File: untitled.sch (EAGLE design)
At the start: 38 parts, among them J2 1x3 RA Female .1", J3 CORTEX_DEBUG_PTH

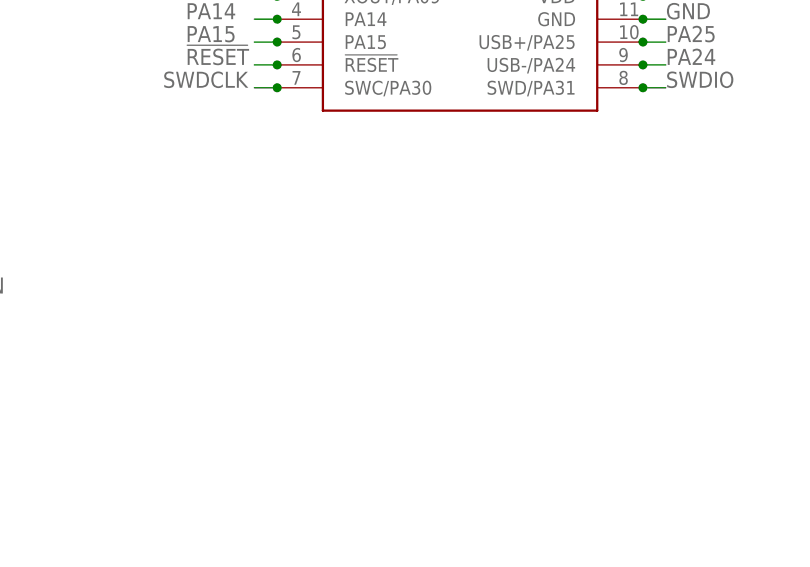
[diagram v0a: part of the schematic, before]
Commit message: Added USB connector
added USB connector for debugging, dropped to 4 layer board
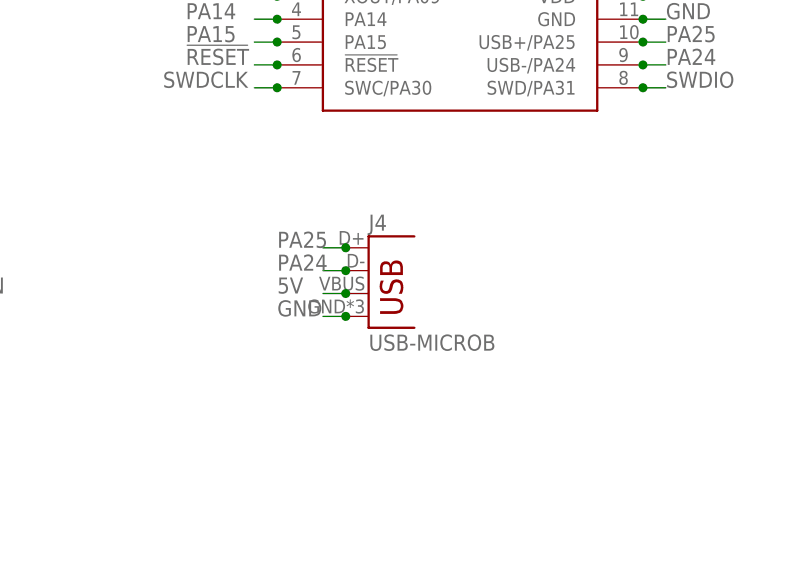
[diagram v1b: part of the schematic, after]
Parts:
- added J4: USB-MICROB, SparkFun-Retired:USB-MICROB
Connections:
- net 5V: now also J4.VBUS
- net GND: now also J4.GND
- net PA24: now also J4.D-
- net PA25: now also J4.D+
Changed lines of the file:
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@@
 <part name="R7" library="resistor" library_urn="urn:adsk.eagle:library:348" deviceset="R-US_" device="R0402" package3d_urn="urn:adsk.eagle:package:26058/1" value="100k"/>
 <part name="L7" library="SparkFun-Coils" library_urn="urn:adsk.eagle:library:512" deviceset="INDUCTOR" device="-0603-33NH" package3d_urn="urn:adsk.eagle:package:37574/1" value="68nH"/>
+<part name="J4" library="SparkFun-Retired" library_urn="urn:adsk.eagle:library:533" deviceset="USB" device="-MICROB"/>
 </parts>
 <sheets>
@@
 <instance part="R7" gate="G$1" x="218.44" y="22.86" rot="R180"/>
 <instance part="L7" gate="G$1" x="266.7" y="68.58" rot="R90"/>
+<instance part="J4" gate="G$1" x="160.02" y="96.52"/>
 </instances>
 <busses>
@@
 <wire x1="271.78" y1="68.58" x2="274.32" y2="68.58" width="0.1524" layer="91"/>
 <junction x="271.78" y="68.58"/>
+</segment>
+<segment>
+<pinref part="J4" gate="G$1" pin="GND"/>
+<wire x1="157.48" y1="96.52" x2="154.94" y2="96.52" width="0.1524" layer="91"/>
+<junction x="157.48" y="96.52"/>
+<label x="149.86" y="96.52" size="1.778" layer="95"/>
 </segment>
 </net>
@@
 <junction x="124.46" y="45.72"/>
 </segment>
+<segment>
+<pinref part="J4" gate="G$1" pin="D+"/>
+<wire x1="157.48" y1="104.14" x2="154.94" y2="104.14" width="0.1524" layer="91"/>
+<junction x="157.48" y="104.14"/>
+<label x="149.86" y="104.14" size="1.778" layer="95"/>
+</segment>
 </net>
 <net name="PA24" class="0">
@@
 <junction x="124.46" y="48.26"/>
 </segment>
+<segment>
+<pinref part="J4" gate="G$1" pin="D-"/>
+<wire x1="157.48" y1="101.6" x2="154.94" y2="101.6" width="0.1524" layer="91"/>
+<junction x="157.48" y="101.6"/>
+<label x="149.86" y="101.6" size="1.778" layer="95"/>
+</segment>
 </net>
 <net name="5V" class="0">
@@
 <junction x="223.52" y="22.86"/>
 </segment>
-</net>
+<segment>
+<pinref part="J4" gate="G$1" pin="VBUS"/>
+<wire x1="157.48" y1="99.06" x2="154.94" y2="99.06" width="0.1524" layer="91"/>
+<junction x="157.48" y="99.06"/>
+<label x="149.86" y="99.06" size="1.778" layer="95"/>
+</segment>
+</net>

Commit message: Added test points to SI4464
Added test points to unused pins for later use. Cleaned up routing.
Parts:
- added TP1, TP2, TP3, TP4, TP5: TEST-POINT3, SparkFun-Connectors:TEST-POINT3
- C1: value (none) -> 12pf
- C2: value (none) -> 470pf
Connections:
- net GPIO0: now also TP2.1
- net GPIO2: now also TP4.1
- net GPIO3: now also TP5.1
- net NIRQ: now also TP3.1
- net TXRAMP: now also TP1.1
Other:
- moved on the sheet: C1, C10, C2, C3, C4, C5, C6, C7, C8, C9, J1, J2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

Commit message: Added 0 ohm resistors to spi
added 0 ohm jumpers between spi pins on the micro and si4464
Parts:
- added R10, R11, R8, R9: 0, resistor:R-US_R0402
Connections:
- new net PA241: R10.1, U$2.SDO
- new net PA251: R11.1, U$2.SCLK
- new net SWDCLK1: R8.1, U$2.NSEL
- new net SWDIO1: R9.1, U$2.SDI
- net PA24: now also R10.2; no longer U$2.SDO
- net PA25: now also R11.2; no longer U$2.SCLK
- net SWDCLK: now also R8.2; no longer U$2.NSEL
- net SWDIO: now also R9.2; no longer U$2.SDI
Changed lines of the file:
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@@
 <part name="TP4" library="SparkFun-Connectors" library_urn="urn:adsk.eagle:library:513" deviceset="TEST-POINT" device="3" package3d_urn="urn:adsk.eagle:package:38286/1"/>
 <part name="TP5" library="SparkFun-Connectors" library_urn="urn:adsk.eagle:library:513" deviceset="TEST-POINT" device="3" package3d_urn="urn:adsk.eagle:package:38286/1"/>
+<part name="R8" library="resistor" library_urn="urn:adsk.eagle:library:348" deviceset="R-US_" device="R0402" package3d_urn="urn:adsk.eagle:package:26058/1" value="0"/>
+<part name="R9" library="resistor" library_urn="urn:adsk.eagle:library:348" deviceset="R-US_" device="R0402" package3d_urn="urn:adsk.eagle:package:26058/1" value="0"/>
+<part name="R10" library="resistor" library_urn="urn:adsk.eagle:library:348" deviceset="R-US_" device="R0402" package3d_urn="urn:adsk.eagle:package:26058/1" value="0"/>
+<part name="R11" library="resistor" library_urn="urn:adsk.eagle:library:348" deviceset="R-US_" device="R0402" package3d_urn="urn:adsk.eagle:package:26058/1" value="0"/>
 </parts>
 <sheets>
@@
 <instance part="TP4" gate="G$1" x="-93.98" y="132.08" rot="R90"/>
 <instance part="TP5" gate="G$1" x="-86.36" y="132.08" rot="R90"/>
+<instance part="R8" gate="G$1" x="-53.34" y="152.4"/>
+<instance part="R9" gate="G$1" x="-53.34" y="144.78"/>
+<instance part="R10" gate="G$1" x="-53.34" y="137.16"/>
+<instance part="R11" gate="G$1" x="-53.34" y="129.54"/>
 </instances>
 <busses>
@@
 </segment>
 <segment>
-<pinref part="U$2" gate="G$1" pin="SDI"/>
-<wire x1="-78.74" y1="185.42" x2="-76.2" y2="185.42" width="0.1524" layer="91"/>
-<label x="-76.2" y="185.42" size="1.778" layer="95"/>
-<junction x="-78.74" y="185.42"/>
+<pinref part="R9" gate="G$1" pin="2"/>
+<wire x1="-48.26" y1="144.78" x2="-45.72" y2="144.78" width="0.1524" layer="91"/>
+<junction x="-48.26" y="144.78"/>
+<label x="-43.18" y="144.78" size="1.778" layer="95"/>
 </segment>
 </net>
@@
 </segment>
 <segment>
-<pinref part="U$2" gate="G$1" pin="NSEL"/>
-<wire x1="-78.74" y1="187.96" x2="-76.2" y2="187.96" width="0.1524" layer="91"/>
-<label x="-76.2" y="187.96" size="1.778" layer="95"/>
-<junction x="-78.74" y="187.96"/>
+<pinref part="R8" gate="G$1" pin="2"/>
+<wire x1="-48.26" y1="152.4" x2="-45.72" y2="152.4" width="0.1524" layer="91"/>
+<junction x="-48.26" y="152.4"/>
+<label x="-43.18" y="152.4" size="1.778" layer="95"/>
 </segment>
 </net>
@@
 </segment>
 <segment>
-<pinref part="U$2" gate="G$1" pin="SCLK"/>
-<wire x1="-78.74" y1="180.34" x2="-76.2" y2="180.34" width="0.1524" layer="91"/>
-<label x="-76.2" y="180.34" size="1.778" layer="95"/>
-<junction x="-78.74" y="180.34"/>
-</segment>
-<segment>
 <pinref part="J4" gate="G$1" pin="D+"/>
 <wire x1="-172.72" y1="33.02" x2="-172.72" y2="35.56" width="0.1524" layer="91"/>
@@
 <label x="-172.72" y="40.64" size="1.778" layer="95" rot="R270"/>
 </segment>
+<segment>
+<pinref part="R11" gate="G$1" pin="2"/>
+<wire x1="-48.26" y1="129.54" x2="-45.72" y2="129.54" width="0.1524" layer="91"/>
+<junction x="-48.26" y="129.54"/>
+<label x="-43.18" y="129.54" size="1.778" layer="95"/>
+</segment>
 </net>
 <net name="PA24" class="0">
@@
 </segment>
 <segment>
-<pinref part="U$2" gate="G$1" pin="SDO"/>
-<wire x1="-78.74" y1="182.88" x2="-76.2" y2="182.88" width="0.1524" layer="91"/>
-<label x="-76.2" y="182.88" size="1.778" layer="95"/>
-<junction x="-78.74" y="182.88"/>
-</segment>
-<segment>
 <pinref part="J4" gate="G$1" pin="D-"/>
 <wire x1="-175.26" y1="33.02" x2="-175.26" y2="35.56" width="0.1524" layer="91"/>
 <junction x="-175.26" y="33.02"/>
 <label x="-175.26" y="40.64" size="1.778" layer="95" rot="R270"/>
+</segment>
+<segment>
+<pinref part="R10" gate="G$1" pin="2"/>
+<wire x1="-48.26" y1="137.16" x2="-45.72" y2="137.16" width="0.1524" layer="91"/>
+<junction x="-48.26" y="137.16"/>
+<label x="-43.18" y="137.16" size="1.778" layer="95"/>
 </segment>
 </net>
@@
 </segment>
 </net>
+<net name="SWDCLK1" class="0">
+<segment>
+<pinref part="U$2" gate="G$1" pin="NSEL"/>
+<wire x1="-78.74" y1="187.96" x2="-76.2" y2="187.96" width="0.1524" layer="91"/>
+<label x="-76.2" y="187.96" size="1.778" layer="95"/>
+<junction x="-78.74" y="187.96"/>
+</segment>
+<segment>
+<pinref part="R8" gate="G$1" pin="1"/>
+<wire x1="-58.42" y1="152.4" x2="-60.96" y2="152.4" width="0.1524" layer="91"/>
+<junction x="-58.42" y="152.4"/>
+<label x="-73.66" y="152.4" size="1.778" layer="95"/>
+</segment>
+</net>
+<net name="SWDIO1" class="0">
+<segment>
+<pinref part="U$2" gate="G$1" pin="SDI"/>
+<wire x1="-78.74" y1="185.42" x2="-76.2" y2="185.42" width="0.1524" layer="91"/>
+<label x="-76.2" y="185.42" size="1.778" layer="95"/>
+<junction x="-78.74" y="185.42"/>
+</segment>
+<segment>
+<pinref part="R9" gate="G$1" pin="1"/>
+<wire x1="-58.42" y1="144.78" x2="-60.96" y2="144.78" width="0.1524" layer="91"/>
+<junction x="-58.42" y="144.78"/>
+<label x="-73.66" y="144.78" size="1.778" layer="95"/>
+</segment>
+</net>
+<net name="PA241" class="0">
+<segment>
+<pinref part="U$2" gate="G$1" pin="SDO"/>
+<wire x1="-78.74" y1="182.88" x2="-76.2" y2="182.88" width="0.1524" layer="91"/>
+<label x="-76.2" y="182.88" size="1.778" layer="95"/>
+<junction x="-78.74" y="182.88"/>
+</segment>
+<segment>
+<pinref part="R10" gate="G$1" pin="1"/>
+<wire x1="-58.42" y1="137.16" x2="-60.96" y2="137.16" width="0.1524" layer="91"/>
+<junction x="-58.42" y="137.16"/>
+<label x="-73.66" y="137.16" size="1.778" layer="95"/>
+</segment>
+</net>
+<net name="PA251" class="0">
+<segment>
+<pinref part="U$2" gate="G$1" pin="SCLK"/>
+<wire x1="-78.74" y1="180.34" x2="-76.2" y2="180.34" width="0.1524" layer="91"/>
+<label x="-76.2" y="180.34" size="1.778" layer="95"/>
+<junction x="-78.74" y="180.34"/>
+</segment>
+<segment>
+<pinref part="R11" gate="G$1" pin="1"/>
+<wire x1="-58.42" y1="129.54" x2="-60.96" y2="129.54" width="0.1524" layer="91"/>
+<junction x="-58.42" y="129.54"/>
+<label x="-73.66" y="129.54" size="1.778" layer="95"/>
+</segment>
+</net>

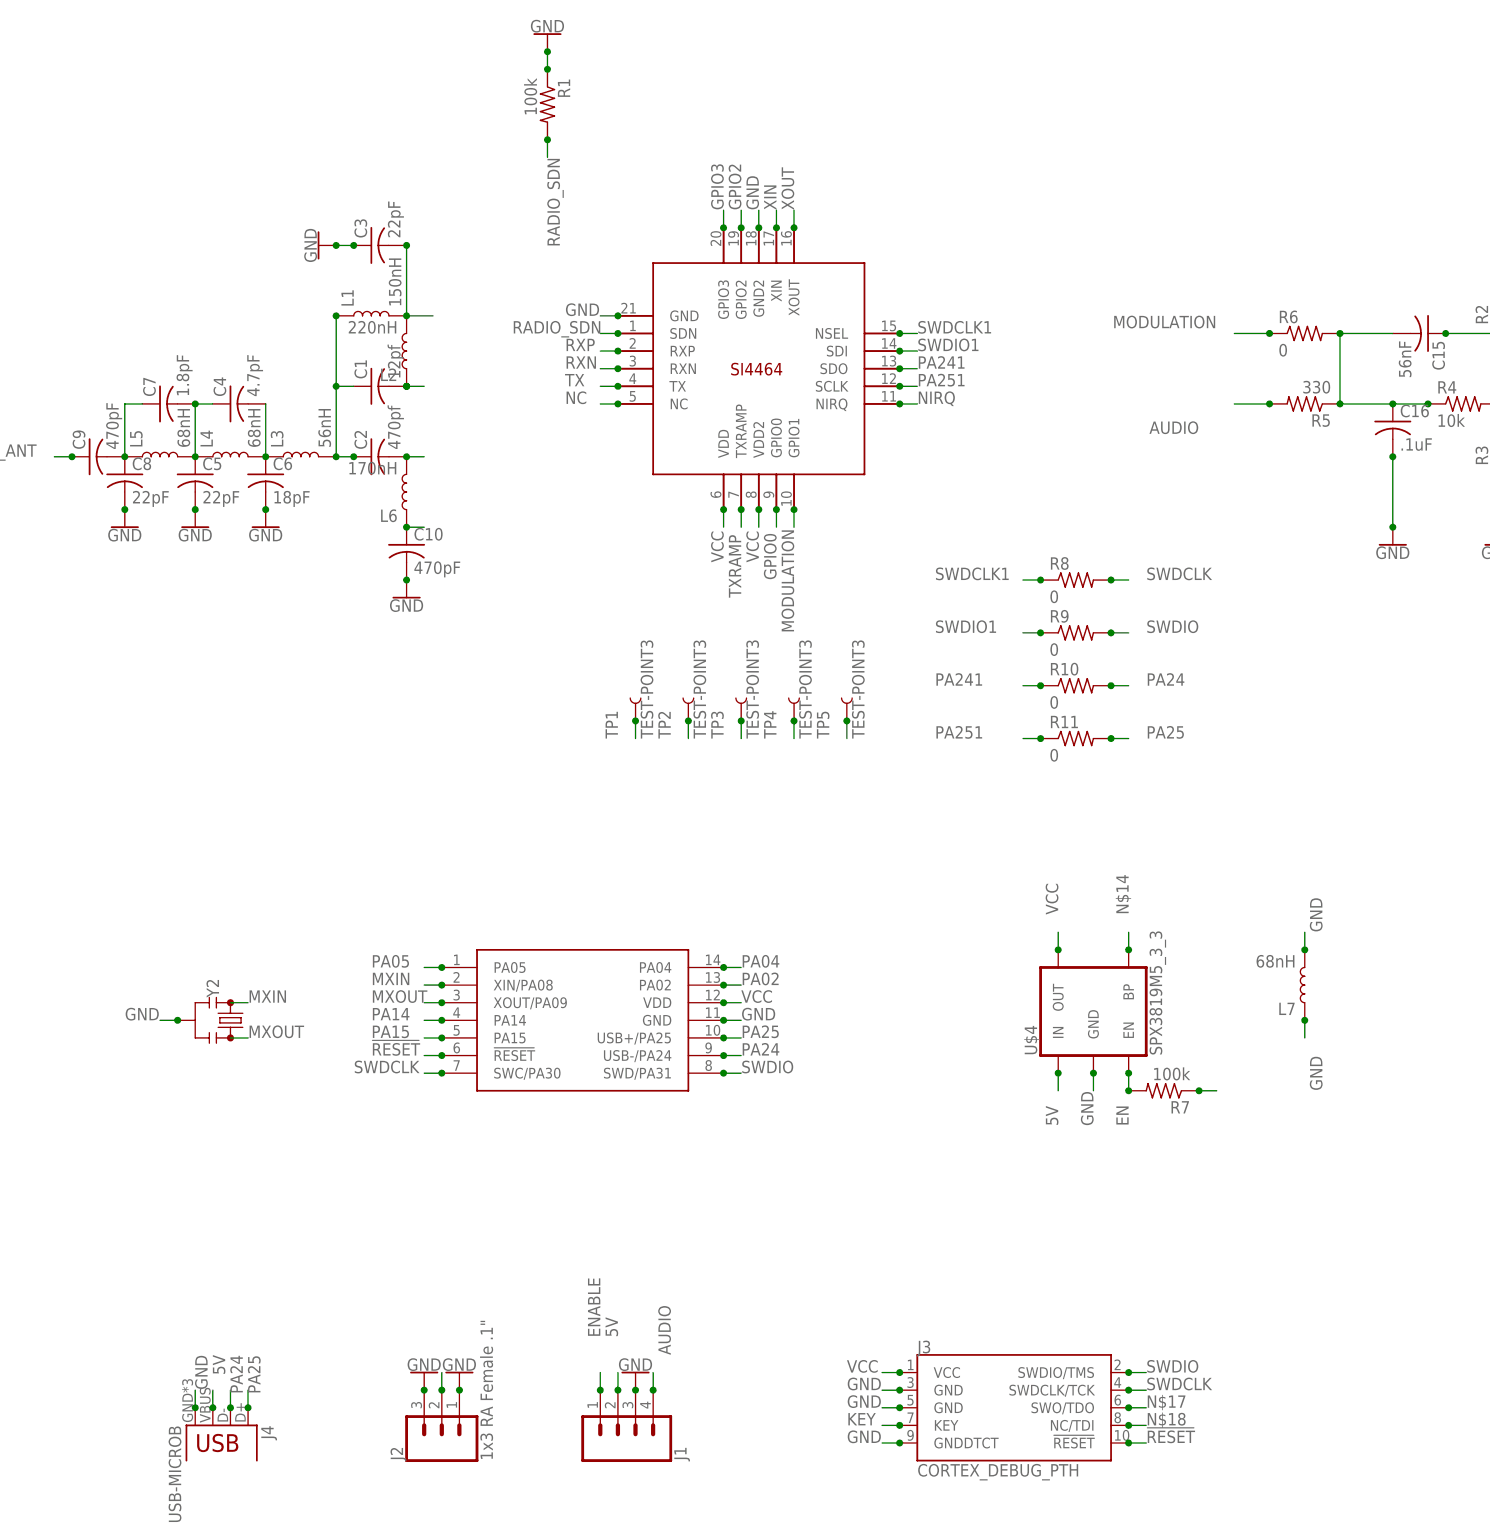
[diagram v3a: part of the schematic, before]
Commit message: saving schematic
eagle error due to inconsistency
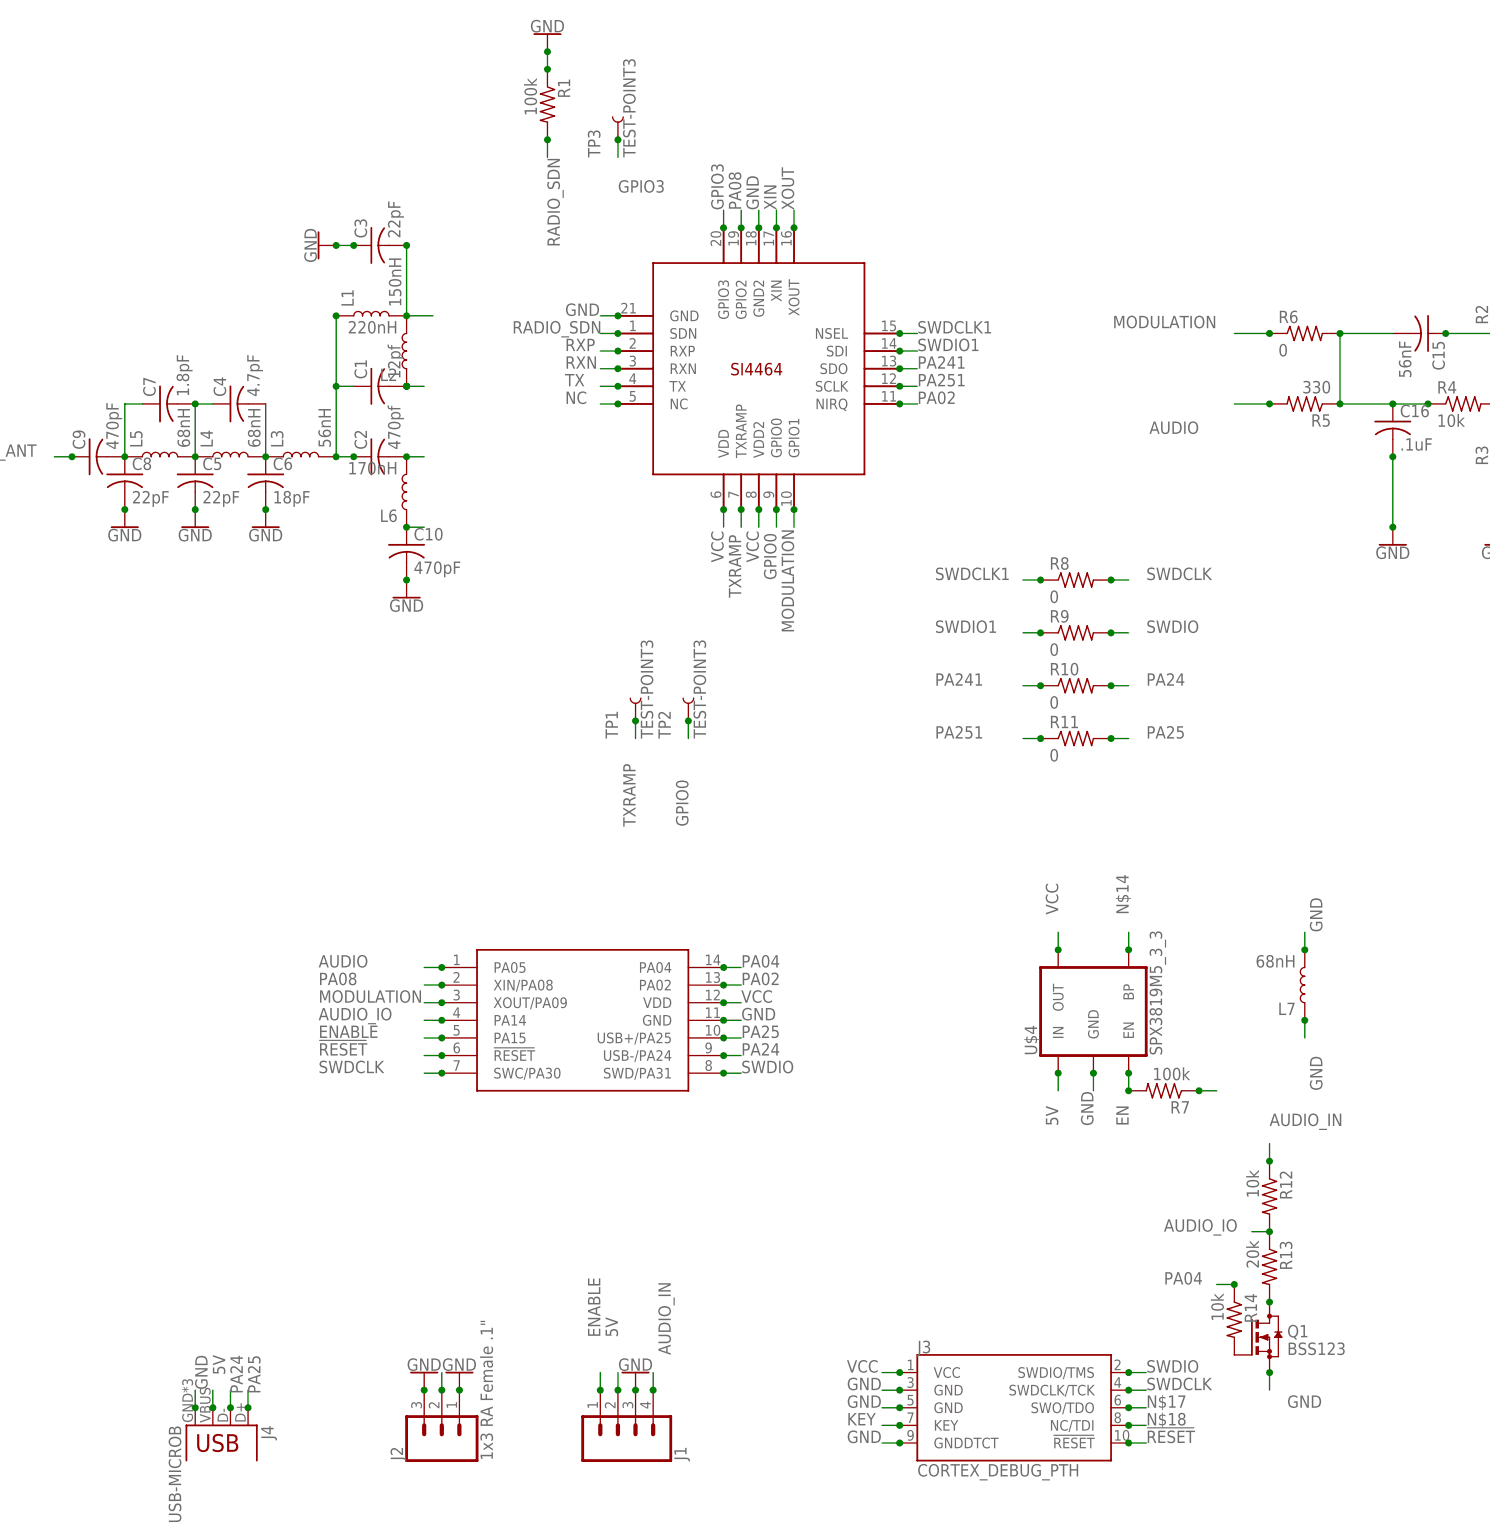
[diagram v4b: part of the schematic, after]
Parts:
- removed TP4, TP5: TEST-POINT3, SparkFun-Connectors:TEST-POINT3
- removed Y2: (no value), SparkFun-Clocks:RESONATORSMD-3.2X1.3
- added Q1: BSS123, transistor-small-signal:BSS123
- added R12, R14: 10k, resistor:R-US_R0402
- added R13: 20k, resistor:R-US_R0402
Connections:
- removed net GPIO2: TP4.1, U$2.GPIO2
- removed net MXIN: U$3.XIN/PA08, Y2.1
- removed net MXOUT: U$3.XOUT/PA09, Y2.3
- removed net NIRQ: TP3.1, U$2.NIRQ
- removed net PA05: U$3.PA05
- removed net PA14: U$3.PA14
- removed net PA15: U$3.PA15
- new net AUDIO_IN: J1.4, R12.1
- new net AUDIO_IO: R12.2, R13.1, U$3.PA14
- new net N$7: Q1.D, R13.2
- new net N$8: Q1.G, R14.2
- new net PA08: U$2.GPIO2, U$3.XIN/PA08
- net AUDIO: now also U$3.PA05; no longer J1.4
- net ENABLE: now also U$3.PA15
- net GND: now also Q1.S; no longer Y2.2
- net GPIO3: now also TP3.1; no longer TP5.1
- net MODULATION: now also U$3.XOUT/PA09
- net PA02: now also U$2.NIRQ
- net PA04: now also R14.1
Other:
- moved on the sheet: TP3
